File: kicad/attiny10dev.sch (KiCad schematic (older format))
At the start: 19 parts, among them J1 Conn_02x06_Odd_Even, J2 Conn_01x06, J3 Conn_01x03_Male, K1 m4-12h, K2 m4-12h, Q1 2N7002, Q2 BSS84, Q3 2N7002, Q4 FZT600, Q5 2N7002, U1 ATtiny10-TS, U2 ATtiny10-TS

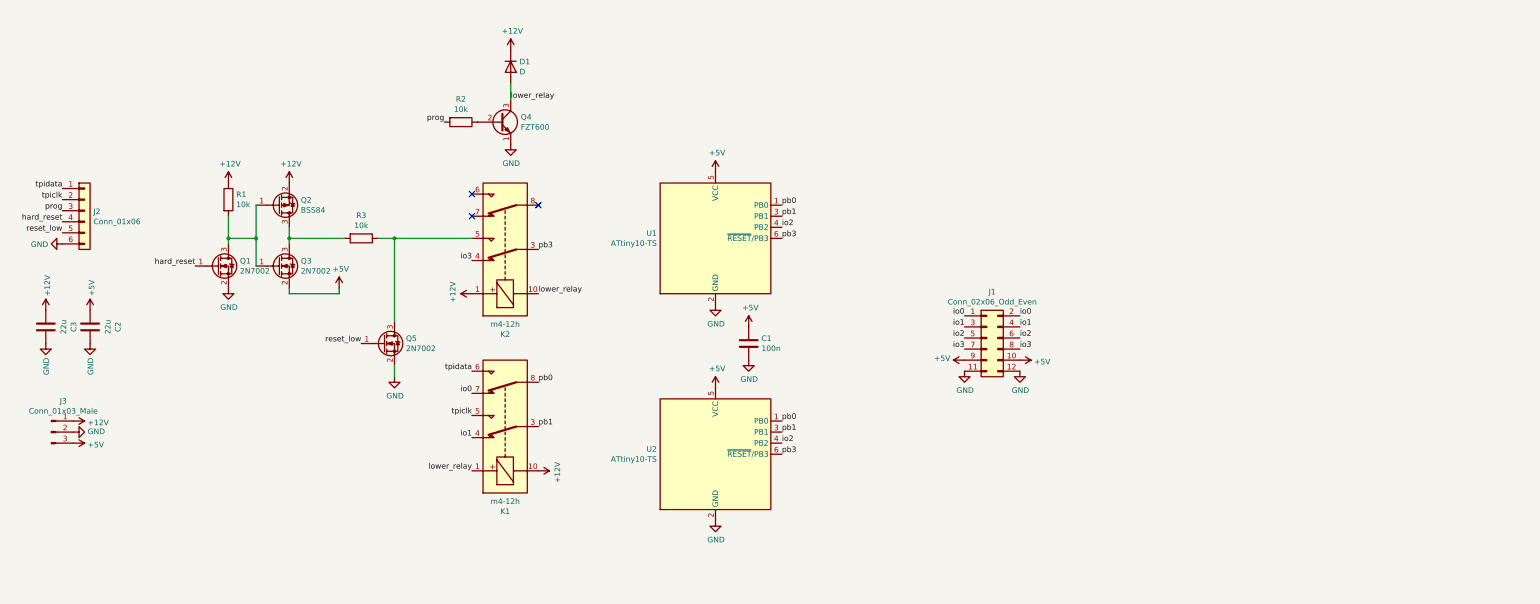
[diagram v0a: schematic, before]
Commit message: Create V2 of shematic
with integrated boost and uC
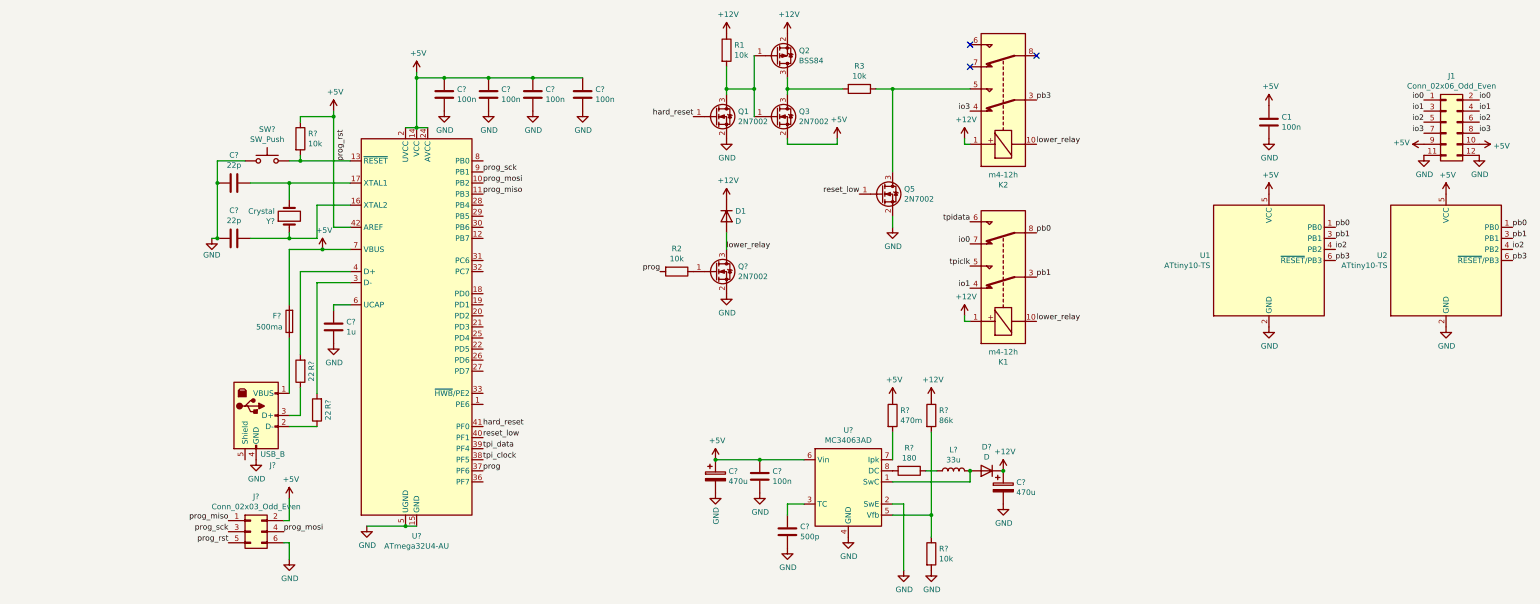
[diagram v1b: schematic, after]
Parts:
- removed C2, C3: 22u, Capacitor_THT:CP_Radial_D12.5mm_P5.00mm, symbol Device:C
- removed J2: Conn_01x06, Connector_PinHeader_2.54mm:PinHeader_1x06_P2.54mm_Vertical, symbol Connector_Generic:Conn_01x06
- removed J3: Conn_01x03_Male, TerminalBlock_RND:TerminalBlock_RND_205-00277_1x03_P5.00mm_Vertical, symbol Connector:Conn_01x03_Male
- removed Q4: FZT600, Package_TO_SOT_THT:TO-92, symbol Transistor_BJT:2N2219
- added C? (x2): 22p, symbol Device:C
- added C?: 1u, symbol Device:C
- added C? (x5): 100n, symbol Device:C
- added C?: 500p, symbol Device:C
- added C? (x2): 470u, symbol Device:CP
- added D?: D, symbol Device:D
- added F?: 500ma, symbol Device:Fuse
- added J?: USB_B, symbol Connector:USB_B
- added J?: Conn_02x03_Odd_Even, symbol Connector_Generic:Conn_02x03_Odd_Even
- added L?: 33u, symbol Device:L
- added Q?: 2N7002, Package_TO_SOT_SMD:SOT-23, symbol Transistor_FET:2N7002
- added R? (x2): 22, symbol Device:R
- added R? (x2): 10k, symbol Device:R
- added R?: 86k, symbol Device:R
- added R?: 470m, symbol Device:R
- added R?: 180, symbol Device:R
- added SW?: SW_Push, symbol Switch:SW_Push
- added U?: MC34063AD, Package_SO:SOIC-8_3.9x4.9mm_P1.27mm, symbol Regulator_Switching:MC34063AD
- added U?: ATmega32U4-AU, Package_QFP:TQFP-44_10x10mm_P0.8mm, symbol MCU_Microchip_ATmega:ATmega32U4-AU
- added Y?: Crystal, symbol Device:Crystal
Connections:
- net +12V: now also K1.1, C?.1, D?.1 (K), R?.1; no longer K1.10
- net +5V: now also C?.1, C?.1, C?.1, C?.1, C?.1, C?.1, F?.2, J?.2 (Pin_2), R?.1, R?.1, U?.14 (VCC), U?.2 (UVCC), U?.24 (AVCC), U?.34 (VCC), U?.42 (AREF), U?.44 (AVCC), U?.6 (Vin), U?.7 (VBUS)
- net GND: now also C?.2, C?.2, C?.2, C?.2, C?.2, C?.2, C?.2, C?.2, C?.2, C?.2, C?.2, J?.4 (GND), J?.6 (Pin_6), Q?.2 (S), R?.2, SW?.1, U?.15 (GND), U?.2 (SwE), U?.23 (GND), U?.35 (GND), U?.4 (GND), U?.43 (GND), U?.5 (UGND)
- net hard_reset: now also U?.41 (PF0)
- net lower_relay: now also K1.10, Q?.3 (D); no longer K1.1
- net prog: now also U?.37 (PF6)
- net reset_low: now also U?.40 (PF1)
- net at R2.1: now also Q?.1 (G)
- new net: D?.2 (A), L?.2, U?.1 (SwC)
- new net: C?.1, U?.3 (TC)
- new net: R?.1, R?.2, U?.5 (Vfb)
- new net: R?.2, U?.7 (Ipk)
- new net: R?.2, U?.8 (DC)
- new net: F?.1, J?.1 (VBUS)
- new net: J?.2 (D-), R?.1
- new net: J?.3 (D+), R?.1
- new net: C?.1, U?.16 (XTAL2), Y?.1
- new net: C?.1, U?.17 (XTAL1), Y?.2
- new net: R?.2, U?.3 (D-)
- new net: R?.2, U?.4 (D+)
- new net: C?.1, U?.6 (UCAP)
- new net: L?.1, R?.1
- new net prog_miso: J?.1 (Pin_1), U?.11 (PB3)
- new net prog_mosi: J?.4 (Pin_4), U?.10 (PB2)
- new net prog_rst: J?.5 (Pin_5), R?.2, SW?.2, U?.13 (~RESET)
- new net prog_sck: J?.3 (Pin_3), U?.9 (PB1)
- new net tpi_clock: U?.38 (PF5)
- new net tpi_data: U?.39 (PF4)
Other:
- moved on the sheet: C1, D1, J1, K1, K2, Q1, Q2, Q3, Q5, R1, R2, R3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

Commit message: Work on next gen pcb
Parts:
- C10, C11, C2, C3, C4, C5, C6, C7, C8: renamed from C?; footprint (none) -> Capacitor_SMD:C_0805_2012Metric_Pad1.15x1.40mm_HandSolder
- C12, C9: renamed from C?; footprint (none) -> Capacitor_THT:CP_Radial_D8.0mm_P5.00mm
- D2: renamed from D?; footprint (none) -> Diode_SMD:D_3220_8050Metric_Pad2.65x5.15mm_HandSolder
- F1: renamed from F?; footprint (none) -> Fuse:Fuse_1206_3216Metric_Pad1.42x1.75mm_HandSolder
- J2: renamed from J?; footprint (none) -> Connector_PinHeader_2.54mm:PinHeader_2x03_P2.54mm_Vertical
- J3: renamed from J?; footprint (none) -> Connector_USB:USB_B_OST_USB-B1HSxx_Horizontal
- L1: renamed from L?; footprint (none) -> Inductor_THT:L_Toroid_Vertical_L13.0mm_W6.5mm_P5.60mm
- R1, R2, R3: footprint Resistor_SMD:R_0805_2012Metric_Pad1.15x1.40mm_HandSolder -> Capacitor_SMD:C_0603_1608Metric_Pad1.05x0.95mm_HandSolder
- R10, R4, R5, R6, R8, R9: renamed from R?; footprint (none) -> Capacitor_SMD:C_0603_1608Metric_Pad1.05x0.95mm_HandSolder
- R7: renamed from R?; footprint (none) -> Resistor_THT:R_Axial_DIN0204_L3.6mm_D1.6mm_P2.54mm_Vertical
- SW1: renamed from SW?; footprint (none) -> Button_Switch_THT:SW_PUSH_6mm
- U4: renamed from U?; footprint Package_SO:SOIC-8_3.9x4.9mm_P1.27mm -> Package_DIP:DIP-8_W10.16mm
- Y1: renamed from Y?; value Crystal -> 16Mhz; footprint (none) -> Crystal:Crystal_SMD_HC49-SD
- gave numbers to parts that had none: 2
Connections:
- net tpiclk is gone; now on net tpi_clk: K1.5
- net tpidata is gone; now on net tpi_data: K1.6
- net GND: now also R2.2
- net prog: now also Q4.1 (G), R2.1; no longer R2.2
- net tpi_clock renamed tpi_clk
- no-connect marks 3 -> 22
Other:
- moved on the sheet: R2

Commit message: V2 of pcb
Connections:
- net io0: now also K1.4; no longer K1.7
- net io1: now also K1.7; no longer K1.4
- net pb0: now also K1.3; no longer K1.8
- net pb1: now also K1.8; no longer K1.3
- net prog: now also U3.39 (PF4); no longer U3.37 (PF6)
- net tpi_clk: now also K1.6, U3.37 (PF6); no longer K1.5, U3.38 (PF5)
- net tpi_data: now also K1.5, U3.38 (PF5); no longer K1.6, U3.39 (PF4)
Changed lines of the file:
@@
 Comment4 ""
 $EndDescr
+Text Label 9150 3000 2    50   ~ 0
+tpi_clk
 Text Label 9150 3400 2    50   ~ 0
-tpi_clk
-Text Label 9150 3000 2    50   ~ 0
 tpi_data
+Text Label 9750 3500 0    50   ~ 0
+pb0
 Text Label 9750 3100 0    50   ~ 0
-pb0
-Text Label 9750 3500 0    50   ~ 0
 pb1
+Text Label 9150 3200 2    50   ~ 0
+io1
 Text Label 9150 3600 2    50   ~ 0
-io1
-Text Label 9150 3200 2    50   ~ 0
 io0
 $Comp
@@
 Text Label 4750 4950 0    50   ~ 0
 reset_low
+Text Label 4750 5150 0    50   ~ 0
+tpi_data
+Text Label 4750 5250 0    50   ~ 0
+tpi_clk
 Text Label 4750 5050 0    50   ~ 0
-tpi_data
-Text Label 4750 5150 0    50   ~ 0
-tpi_clk
-Text Label 4750 5250 0    50   ~ 0
 prog
 Text Label 4750 2550 0    50   ~ 0

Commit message: Finalize rev 2 pcb
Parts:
- added TP1, TP2, TP3, TP4, TP5: TestPoint, TestPoint:TestPoint_THTPad_D1.0mm_Drill0.5mm, symbol Connector:TestPoint
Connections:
- net +12V: now also TP1.1
- net io2: now also TP4.1
- net pb0: now also TP2.1
- net pb1: now also TP3.1
- net pb3: now also TP5.1
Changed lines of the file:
@@
 Connection ~ 6650 3450
 NoConn ~ 2600 5150
+$Comp
+L Connector:TestPoint TP1
+U 1 1 603EA418
+P 11200 4850
+F 0 "TP1" V 11154 5038 50  0000 L CNN
+F 1 "TestPoint" V 11245 5038 50  0000 L CNN
+F 2 "TestPoint:TestPoint_THTPad_D1.0mm_Drill0.5mm" H 11400 4850 50  0001 C CNN
+F 3 "~" H 11400 4850 50  0001 C CNN
+	1    11200 4850
+	0    1    1    0
+$EndComp
+$Comp
+L Connector:TestPoint TP2
+U 1 1 603F4857
+P 11200 5050
+F 0 "TP2" V 11154 5238 50  0000 L CNN
+F 1 "TestPoint" V 11245 5238 50  0000 L CNN
+F 2 "TestPoint:TestPoint_THTPad_D1.0mm_Drill0.5mm" H 11400 5050 50  0001 C CNN
+F 3 "~" H 11400 5050 50  0001 C CNN
+	1    11200 5050
+	0    1    1    0
+$EndComp
+$Comp
+L Connector:TestPoint TP3
+U 1 1 603F5D45
+P 11200 5250
+F 0 "TP3" V 11154 5438 50  0000 L CNN
+F 1 "TestPoint" V 11245 5438 50  0000 L CNN
+F 2 "TestPoint:TestPoint_THTPad_D1.0mm_Drill0.5mm" H 11400 5250 50  0001 C CNN
+F 3 "~" H 11400 5250 50  0001 C CNN
+	1    11200 5250
+	0    1    1    0
+$EndComp
+$Comp
+L Connector:TestPoint TP4
+U 1 1 603F5D4B
+P 11200 5450
+F 0 "TP4" V 11154 5638 50  0000 L CNN
+F 1 "TestPoint" V 11245 5638 50  0000 L CNN
+F 2 "TestPoint:TestPoint_THTPad_D1.0mm_Drill0.5mm" H 11400 5450 50  0001 C CNN
+F 3 "~" H 11400 5450 50  0001 C CNN
+	1    11200 5450
+	0    1    1    0
+$EndComp
+$Comp
+L power:+12V #PWR0103
+U 1 1 603F7ACB
+P 11200 4850
+F 0 "#PWR0103" H 11200 4700 50  0001 C CNN
+F 1 "+12V" H 11215 5023 50  0000 C CNN
+F 2 "" H 11200 4850 50  0001 C CNN
+F 3 "" H 11200 4850 50  0001 C CNN
+	1    11200 4850
+	1    0    0    -1
+$EndComp
+$Comp
+L Connector:TestPoint TP5
+U 1 1 603FD2FA
+P 11200 5650
+F 0 "TP5" V 11154 5838 50  0000 L CNN
+F 1 "TestPoint" V 11245 5838 50  0000 L CNN
+F 2 "TestPoint:TestPoint_THTPad_D1.0mm_Drill0.5mm" H 11400 5650 50  0001 C CNN
+F 3 "~" H 11400 5650 50  0001 C CNN
+	1    11200 5650
+	0    1    1    0
+$EndComp
+Text Label 11200 5050 2    50   ~ 0
+pb0
+Text Label 11200 5250 2    50   ~ 0
+pb1
+Text Label 11200 5450 2    50   ~ 0
+io2
+Text Label 11200 5650 2    50   ~ 0
+pb3
 $EndSCHEMATC

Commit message: Fix boost
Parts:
- K1, K2: symbol random_things:m4-12h -> attiny10dev-rescue:m4-12h-random_things
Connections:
- net at R10.1, R9.2, U4.5 (Vfb): now also R7.2, U4.7 (Ipk)
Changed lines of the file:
@@
 io0
 $Comp
-L random_things:m4-12h K1
+L attiny10dev-rescue:m4-12h-random_things K1
 U 1 1 5F40FC98
 P 9450 3500
@@
 lower_relay
 $Comp
-L random_things:m4-12h K2
+L attiny10dev-rescue:m4-12h-random_things K2
 U 1 1 5F422885
 P 9450 1900
@@
 	0    1    1    0
 $EndComp
-Wire Wire Line
-	8450 5650 8800 5650
 $Comp
 L power:+5V #PWR037
@@
 $EndComp
 Wire Wire Line
-	8450 4900 8450 5150
+	8450 4900 8450 4950
 $Comp
 L Device:R R7
@@
 	1    0    0    -1
 $EndComp
-Connection ~ 8800 5650
 Wire Wire Line
 	8800 5650 8800 5850
-Wire Wire Line
-	8800 5650 8800 4900
 Wire Wire Line
 	7500 5550 7650 5550
@@
 Text Label 11200 5650 2    50   ~ 0
 pb3
+Connection ~ 8800 5650
+Wire Wire Line
+	8450 5650 8800 5650
+Wire Wire Line
+	8800 5650 8800 4950
+Wire Wire Line
+	8450 4950 8800 4950
+Connection ~ 8450 4950
+Wire Wire Line
+	8450 4950 8450 5150
+Connection ~ 8800 4950
+Wire Wire Line
+	8800 4950 8800 4900
 $EndSCHEMATC
